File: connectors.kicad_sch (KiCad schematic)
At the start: 6 parts

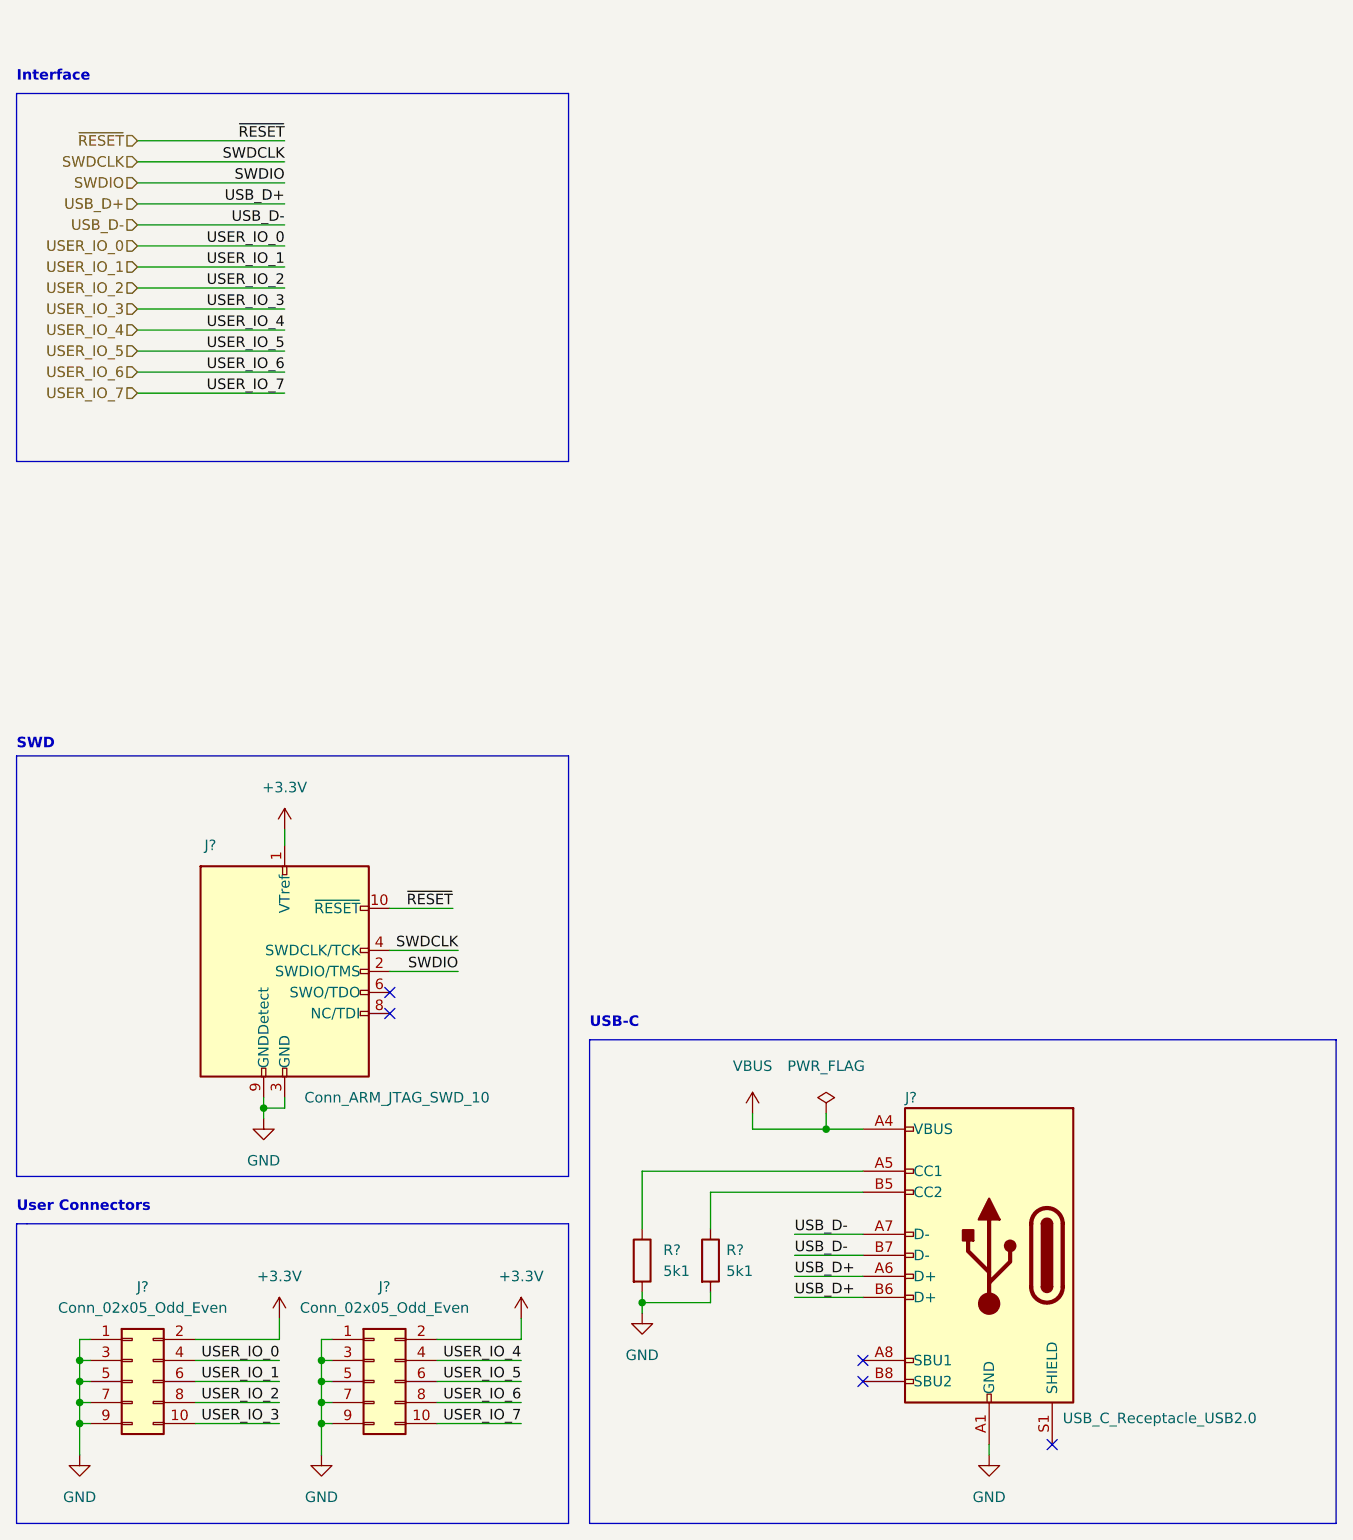
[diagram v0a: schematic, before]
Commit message: All component except led matrix
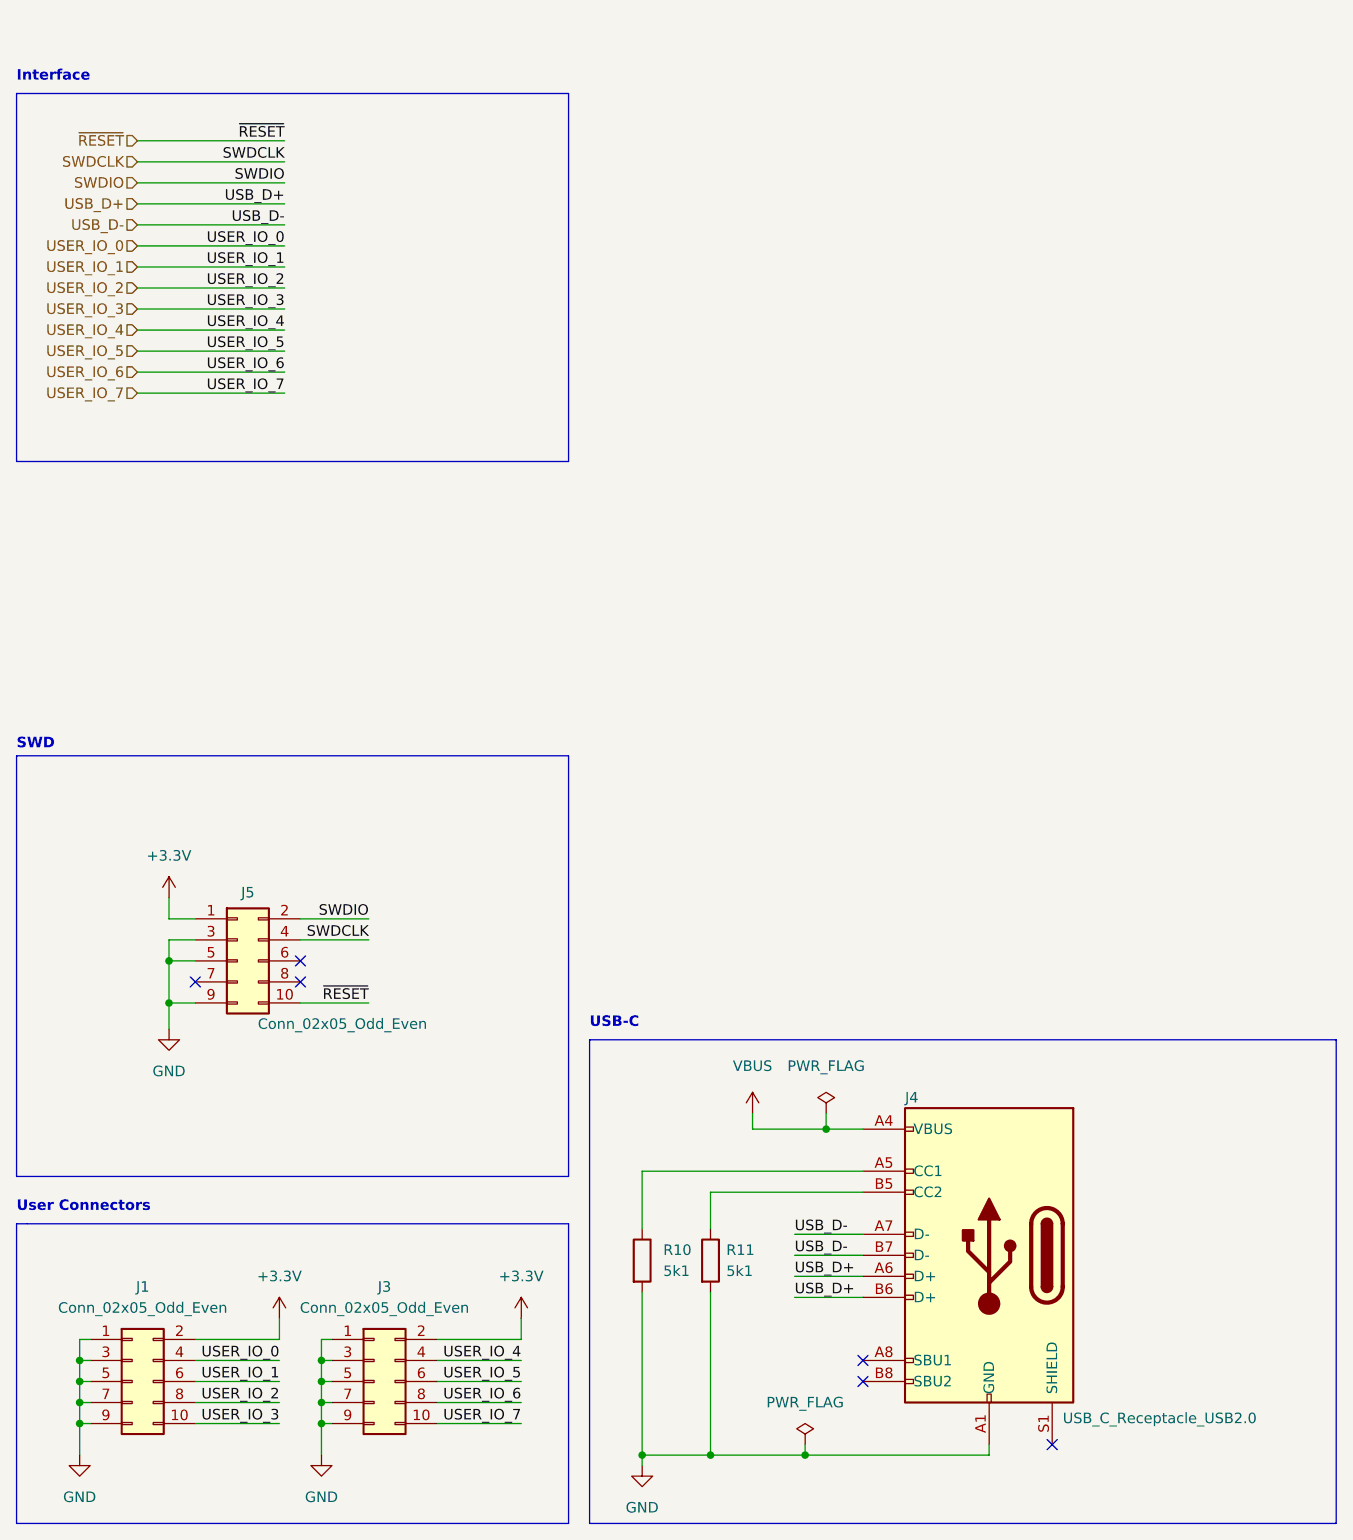
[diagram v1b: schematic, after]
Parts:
- removed J?: Conn_ARM_JTAG_SWD_10, symbol Connector:Conn_ARM_JTAG_SWD_10
- added J5: Conn_02x05_Odd_Even, symbol Connector_Generic:Conn_02x05_Odd_Even
- gave numbers to parts that had none: 5
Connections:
- net +3V3: now also J5.1 (Pin_1)
- net GND: now also J5.3 (Pin_3), J5.5 (Pin_5), J5.9 (Pin_9)
- net SWDCLK: now also J5.4 (Pin_4)
- net SWDIO: now also J5.2 (Pin_2)
- net ~{RESET}: now also J5.10 (Pin_10)
- no-connect marks 5 -> 6

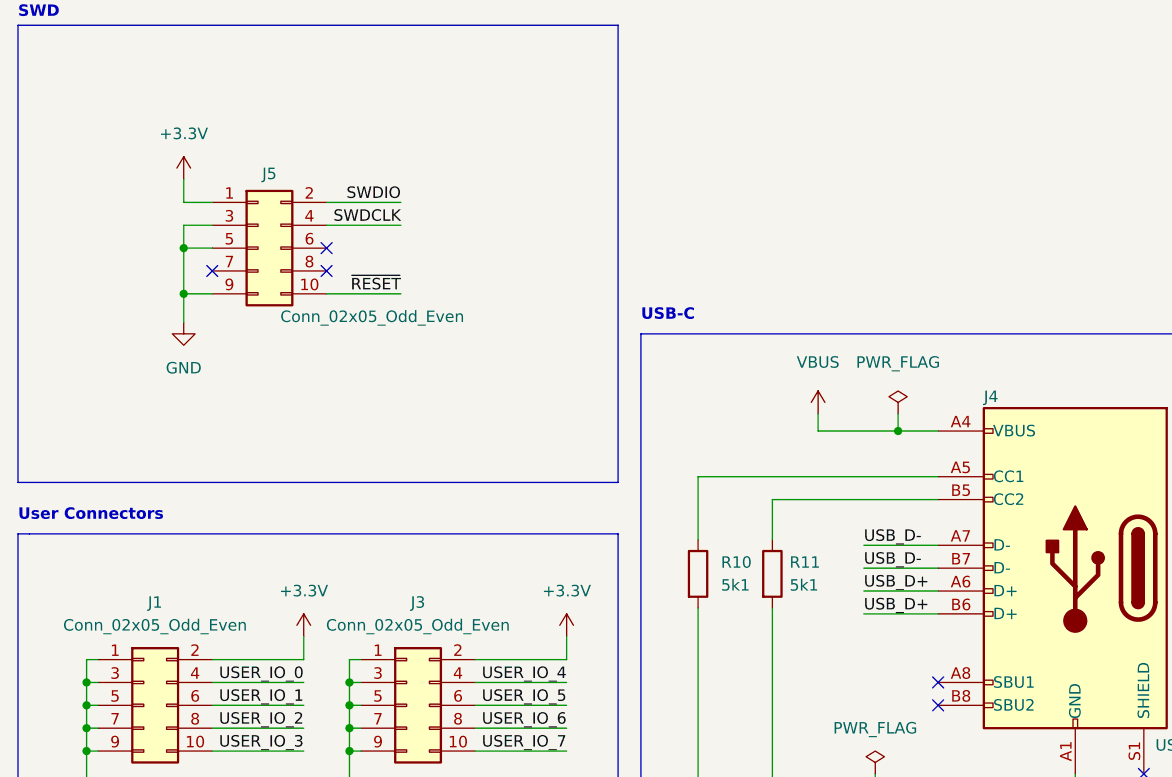
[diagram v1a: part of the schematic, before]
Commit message: finish schematic, prep pcb
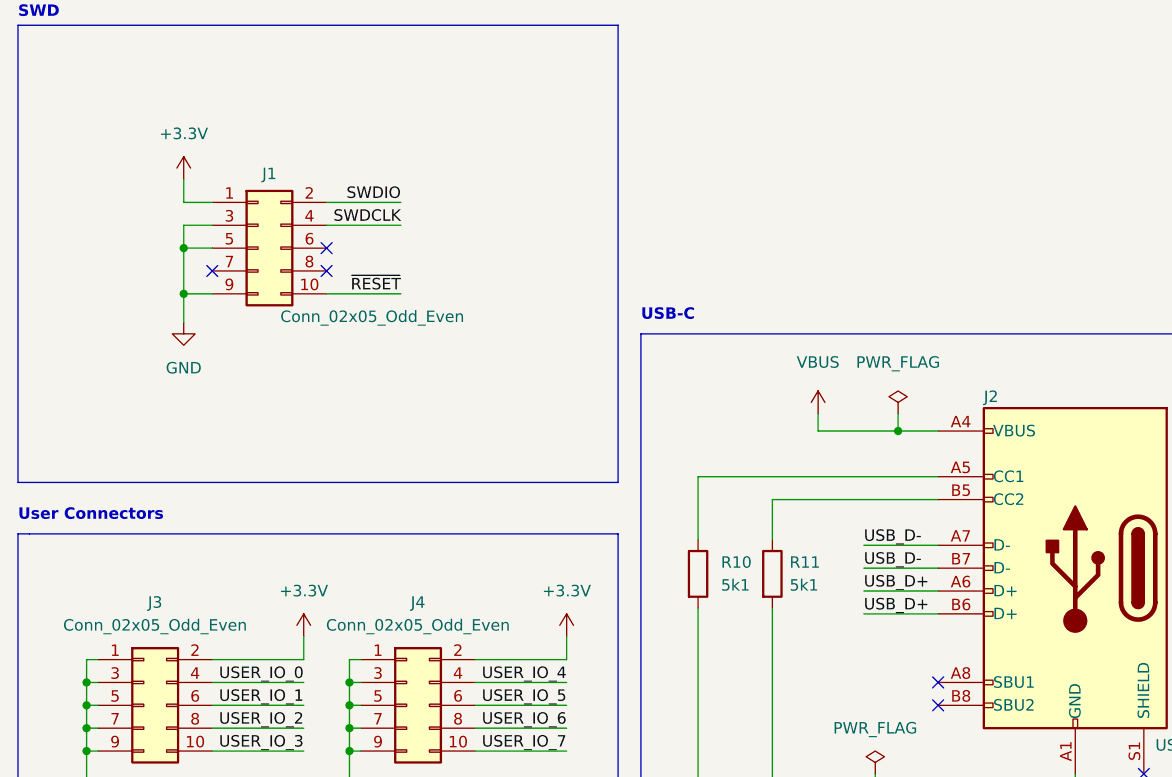
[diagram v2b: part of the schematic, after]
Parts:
- J1: renamed from J5; footprint (none) -> Connector:Tag-Connect_TC2050-IDC-FP_2x05_P1.27mm_Vertical
- J2: renamed from J4; footprint (none) -> Connector_USB:USB_C_Receptacle_Palconn_UTC16-G
- J3: renamed from J1; footprint (none) -> Connector_Hirose:Hirose_DF12_DF12C3.0-10DS-0.5V_2x05_P0.50mm_Vertical
- J4: renamed from J3; footprint (none) -> Connector_Hirose:Hirose_DF12_DF12C3.0-10DS-0.5V_2x05_P0.50mm_Vertical
- R10, R11: footprint (none) -> Resistor_SMD:R_0402_1005Metric
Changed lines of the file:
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@@
       (effects (font (size 1.27 1.27)) (justify left))
     )
-    (property "Footprint" "" (id 2) (at 96.647 163.195 90)
+    (property "Footprint" "Resistor_SMD:R_0402_1005Metric" (id 2) (at 96.647 163.195 90)
       (effects (font (size 1.27 1.27)) hide)
     )
@@
   (symbol (lib_id "Connector_Generic:Conn_02x05_Odd_Even") (at 28.575 177.8 0) (unit 1)
     (in_bom yes) (on_board yes) (fields_autoplaced)
-    (property "Reference" "J1" (id 0) (at 29.845 166.37 0))
+    (property "Reference" "J3" (id 0) (at 29.845 166.37 0))
     (property "Value" "Conn_02x05_Odd_Even" (id 1) (at 29.845 168.91 0))
-    (property "Footprint" "" (id 2) (at 28.575 177.8 0)
+    (property "Footprint" "Connector_Hirose:Hirose_DF12_DF12C3.0-10DS-0.5V_2x05_P0.50mm_Vertical" (id 2) (at 28.575 177.8 0)
       (effects (font (size 1.27 1.27)) hide)
     )
@@
   (symbol (lib_id "power:GND") (at 33.02 135.255 0) (unit 1)
     (in_bom yes) (on_board yes) (fields_autoplaced)
-    (property "Reference" "#PWR0126" (id 0) (at 33.02 141.605 0)
+    (property "Reference" "#PWR074" (id 0) (at 33.02 141.605 0)
       (effects (font (size 1.27 1.27)) hide)
     )
@@
   (symbol (lib_id "power:+3.3V") (at 33.02 119.38 0) (unit 1)
     (in_bom yes) (on_board yes) (fields_autoplaced)
-    (property "Reference" "#PWR0127" (id 0) (at 33.02 123.19 0)
+    (property "Reference" "#PWR073" (id 0) (at 33.02 123.19 0)
       (effects (font (size 1.27 1.27)) hide)
     )
@@
   (symbol (lib_id "power:PWR_FLAG") (at 112.395 145.415 0) (unit 1)
     (in_bom yes) (on_board yes) (fields_autoplaced)
-    (property "Reference" "#FLG0101" (id 0) (at 112.395 143.51 0)
+    (property "Reference" "#FLG02" (id 0) (at 112.395 143.51 0)
       (effects (font (size 1.27 1.27)) hide)
     )
@@
   (symbol (lib_id "power:PWR_FLAG") (at 109.855 185.42 0) (unit 1)
     (in_bom yes) (on_board yes) (fields_autoplaced)
-    (property "Reference" "#FLG0102" (id 0) (at 109.855 183.515 0)
+    (property "Reference" "#FLG03" (id 0) (at 109.855 183.515 0)
       (effects (font (size 1.27 1.27)) hide)
     )
@@
   (symbol (lib_id "power:GND") (at 22.225 186.69 0) (unit 1)
     (in_bom yes) (on_board yes) (fields_autoplaced)
-    (property "Reference" "#PWR0125" (id 0) (at 22.225 193.04 0)
+    (property "Reference" "#PWR078" (id 0) (at 22.225 193.04 0)
       (effects (font (size 1.27 1.27)) hide)
     )
@@
   (symbol (lib_id "power:GND") (at 51.435 186.69 0) (unit 1)
     (in_bom yes) (on_board yes) (fields_autoplaced)
-    (property "Reference" "#PWR0128" (id 0) (at 51.435 193.04 0)
+    (property "Reference" "#PWR079" (id 0) (at 51.435 193.04 0)
       (effects (font (size 1.27 1.27)) hide)
     )
@@
   (symbol (lib_id "Connector_Generic:Conn_02x05_Odd_Even") (at 41.275 127 0) (unit 1)
     (in_bom yes) (on_board yes)
-    (property "Reference" "J5" (id 0) (at 42.545 118.745 0))
+    (property "Reference" "J1" (id 0) (at 42.545 118.745 0))
     (property "Value" "Conn_02x05_Odd_Even" (id 1) (at 53.975 134.62 0))
-    (property "Footprint" "" (id 2) (at 41.275 127 0)
+    (property "Footprint" "Connector:Tag-Connect_TC2050-IDC-FP_2x05_P1.27mm_Vertical" (id 2) (at 41.275 127 0)
       (effects (font (size 1.27 1.27)) hide)
     )
@@
       (effects (font (size 1.27 1.27)) (justify left))
     )
-    (property "Footprint" "" (id 2) (at 88.392 163.195 90)
+    (property "Footprint" "Resistor_SMD:R_0402_1005Metric" (id 2) (at 88.392 163.195 90)
       (effects (font (size 1.27 1.27)) hide)
     )
@@
   (symbol (lib_id "Connector:USB_C_Receptacle_USB2.0") (at 132.08 162.56 0) (mirror y) (unit 1)
     (in_bom yes) (on_board yes)
-    (property "Reference" "J4" (id 0) (at 121.92 143.51 0)
+    (property "Reference" "J2" (id 0) (at 121.92 143.51 0)
       (effects (font (size 1.27 1.27)) (justify right))
     )
@@
       (effects (font (size 1.27 1.27)) (justify right))
     )
-    (property "Footprint" "" (id 2) (at 128.27 162.56 0)
+    (property "Footprint" "Connector_USB:USB_C_Receptacle_Palconn_UTC16-G" (id 2) (at 128.27 162.56 0)
       (effects (font (size 1.27 1.27)) hide)
     )
@@
   (symbol (lib_id "power:+3.3V") (at 75.565 170.18 0) (unit 1)
     (in_bom yes) (on_board yes) (fields_autoplaced)
-    (property "Reference" "#PWR0130" (id 0) (at 75.565 173.99 0)
+    (property "Reference" "#PWR077" (id 0) (at 75.565 173.99 0)
       (effects (font (size 1.27 1.27)) hide)
     )
@@
   (symbol (lib_id "Connector_Generic:Conn_02x05_Odd_Even") (at 57.785 177.8 0) (unit 1)
     (in_bom yes) (on_board yes) (fields_autoplaced)
-    (property "Reference" "J3" (id 0) (at 59.055 166.37 0))
+    (property "Reference" "J4" (id 0) (at 59.055 166.37 0))
     (property "Value" "Conn_02x05_Odd_Even" (id 1) (at 59.055 168.91 0))
-    (property "Footprint" "" (id 2) (at 57.785 177.8 0)
+    (property "Footprint" "Connector_Hirose:Hirose_DF12_DF12C3.0-10DS-0.5V_2x05_P0.50mm_Vertical" (id 2) (at 57.785 177.8 0)
       (effects (font (size 1.27 1.27)) hide)
     )
@@
   (symbol (lib_id "power:+3.3V") (at 46.355 170.18 0) (unit 1)
     (in_bom yes) (on_board yes) (fields_autoplaced)
-    (property "Reference" "#PWR0129" (id 0) (at 46.355 173.99 0)
+    (property "Reference" "#PWR076" (id 0) (at 46.355 173.99 0)
       (effects (font (size 1.27 1.27)) hide)
     )
@@
   (symbol (lib_id "power:VBUS") (at 103.505 145.415 0) (unit 1)
     (in_bom yes) (on_board yes) (fields_autoplaced)
-    (property "Reference" "#PWR0123" (id 0) (at 103.505 149.225 0)
+    (property "Reference" "#PWR075" (id 0) (at 103.505 149.225 0)
       (effects (font (size 1.27 1.27)) hide)
     )
@@
   (symbol (lib_id "power:GND") (at 90.17 187.96 0) (unit 1)
     (in_bom yes) (on_board yes) (fields_autoplaced)
-    (property "Reference" "#PWR0122" (id 0) (at 90.17 194.31 0)
-      (effects (font (size 1.27 1.27)) hide)
-    )
+    (property "Reference" "#PWR080" (id 0) (at 90.17 194.31 0)
+      (effects (font (size 1.27 1.27)) hide)
+    )
